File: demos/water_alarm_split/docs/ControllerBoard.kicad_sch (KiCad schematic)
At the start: 4 parts, among them U1 SN74HC04, U2 CD4069

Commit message: export: kicad_sch — Phase 2.5b: layered placement, wire routing, KiCad 10 compatibility (#23)
* export: kicad_sch — Phase 2.5b: layered placement + routing + KiCad 9 fix

Placement (placement.py, complete rewrite):
- Replaces naive grid with Layered Signal Flow algorithm (spec §5 stages 1–8)
- Stage 1: band classification — power chips/rails at top, LEDs at bottom,
  everything else in the signal band
- Stage 2: signal-flow DAG via BFS from Rail/Connector sources; layer = BFS
  distance from nearest source
- Stage 3–4: place within (band, layer) cells at 1500-mil (38.1 mm) same-band
  spacing, 1000-mil inter-band gutter, 25.4 mm page margin
- Stage 6: cluster breakup — up to 10 iterations shifting same-band parts
  that land closer than 0.9× SAME_BAND_SPACING_MM
- Stage 8: page sized to fit (A4 → A3 → A2 → A1)
- grid_place() and sheet_size_mm() kept as shims for backward-compat

Routing (routing.py, new file):
- route_net(): connects stub ends with Manhattan L-shapes (horizontal first)
- find_junctions(): returns points where ≥3 wire endpoints coincide
- renderer uses routed wires between signal-net stub ends

Hierarchical (hierarchical.py, new file):
- collect_boards(), is_multi_board(), sub_sheet_filename() — interface stub
  for multi-Board sub-sheet emission (full implementation deferred)

KiCad 9 sub-symbol name fix (library_loader.py):
- KiCad 9 schematics expect sub-symbols nested inside their parent in
  lib_symbols to use the bare name (R_0_1, LED_0_1, 4069_1_0) — NOT the
  lib-qualified name (Device:R_0_1, Device:LED_0_1, 4xxx:4069_1_0)
- Fixed _qualify_names() to add the lib: prefix only to the exact parent
  symbol name using a lookahead (?=") that prevents sub-unit names from
  being qualified

Tests (+25 tests):
- test_placement.py: band classification, all-on-grid, determinism,
  minimum spacing, power < signal < indicator Y ordering, page sizing
- test_routing.py: H/V segments, L-shapes, orthogonality, grid snap,
  junction detection

Golden files re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
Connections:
- net Net-(D2-anode): now also D2.2 (A)
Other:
- moved on the sheet: D1, D2, U1A, U2A

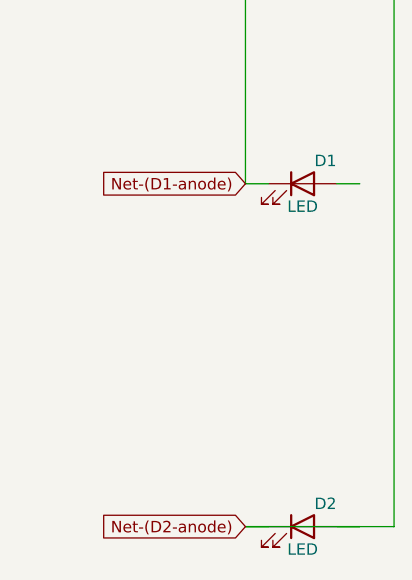
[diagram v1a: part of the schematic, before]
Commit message: framework: LED.cathode mandatory + close WaterAlarm regression (#29)
Found while reviewing WaterAlarm's breadboard SVG: the LEDs in the
design had no ground connections drawn. Investigation revealed
`LED.cathode` was declared `mandatory=False` with the docstring claim
*"floating = GND"* — a "structurally inert under graph evaluation"
shortcut that lets demos write electrically-broken circuits and have
them pass ERC.

A real LED with a dangling cathode does not light. This is exactly
the kind of physical-fidelity violation `CLAUDE.md` lists as
disallowed.

  - `src/components/passives/led.py`: `cathode` becomes
    `mandatory=True`. Docstring updated to drop the "floating = GND"
    claim and explain the contract.
  - `tests/components/test_led.py`: regression tests pin both ports
    as mandatory and confirm `Circuit.__init__` raises
    `UnconnectedPinError` end-to-end when a cathode is left
    floating.
  - `demos/water_alarm/water_alarm.py` and
    `demos/water_alarm_split/water_alarm_split.py`: cathodes wired
    to the GND rail. (Bench builds still need a series current-limit
    resistor; the logic-level demo doesn't model V_F or current.)
  - `tests/framework/test_circuit_autocollect.py`,
    `tests/framework/test_framework.py`, and
    `tests/framework/import_kicad/test_import.py`: fixtures that
    leaned on the broken default updated so they still pin down the
    specific error each test exists to catch.
  - Demo docs regenerated for the two WaterAlarm variants.
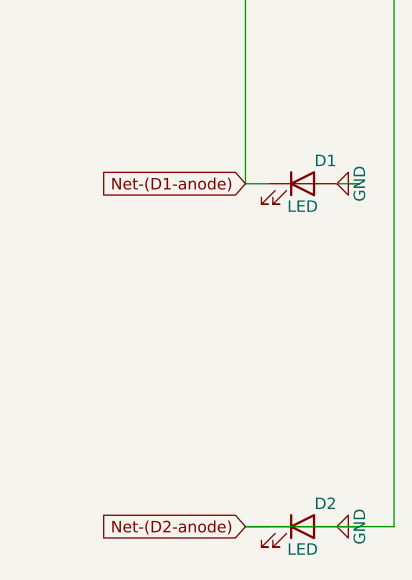
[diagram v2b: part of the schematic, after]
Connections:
- net Net-(D2-anode) is gone; now on net GND: D2.1 (K), D2.2 (A), U2.2
- net GND: now also D1.2 (A)
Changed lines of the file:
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@@
+  )
+  (symbol
+    (lib_id "power:GND")
+    (at 69.85 927.1 270)
+    (unit 1)
+    (exclude_from_sim no)
+    (in_bom yes)
+    (on_board yes)
+    (dnp no)
+    (property "Reference" "#PWR"
+      (at 69.85 927.1 0)
+      (effects (font (size 1.27 1.27)) (hide yes))
+    )
+    (property "Value" "GND"
+      (at 69.85 927.1 0)
+      (effects (font (size 1.27 1.27)))
+    )
+    (pin "1")
   )
   (symbol
@@
     (stroke (width 0) (type default))
   )
+  (symbol
+    (lib_id "power:GND")
+    (at 69.85 965.2 270)
+    (unit 1)
+    (exclude_from_sim no)
+    (in_bom yes)
+    (on_board yes)
+    (dnp no)
+    (property "Reference" "#PWR"
+      (at 69.85 965.2 0)
+      (effects (font (size 1.27 1.27)) (hide yes))
+    )
+    (property "Value" "GND"
+      (at 69.85 965.2 0)
+      (effects (font (size 1.27 1.27)))
+    )
+    (pin "1")
+  )
   (wire
